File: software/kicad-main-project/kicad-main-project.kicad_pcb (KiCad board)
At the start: 2 copper layers, 1 part, among them U1 ESP32-DevKitC

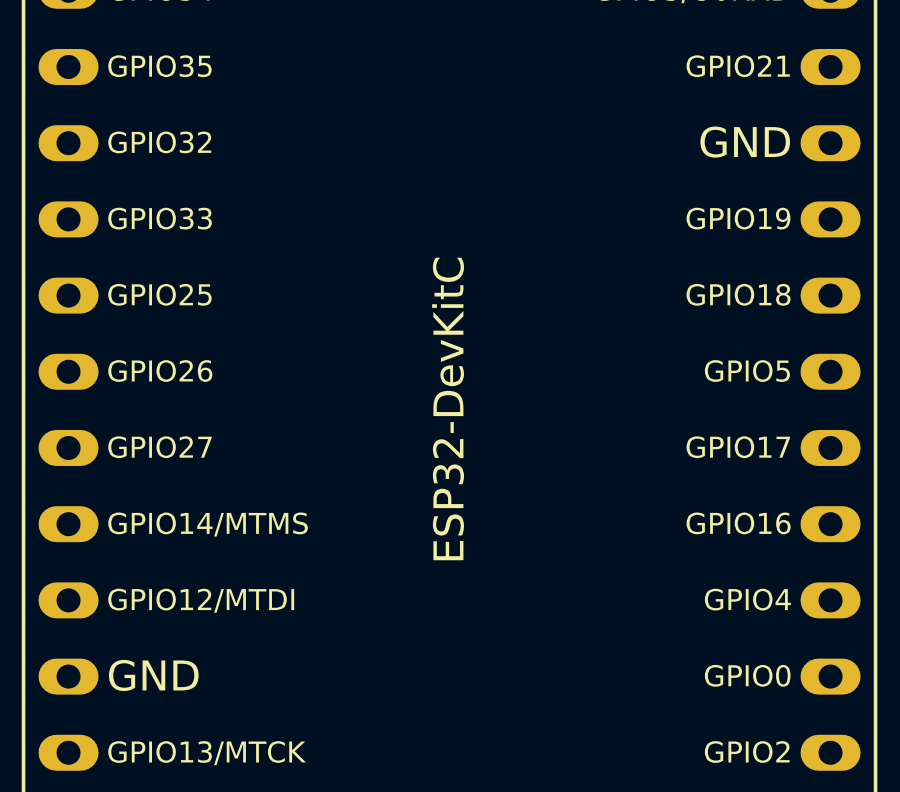
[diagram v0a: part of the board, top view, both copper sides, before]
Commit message: update schematic
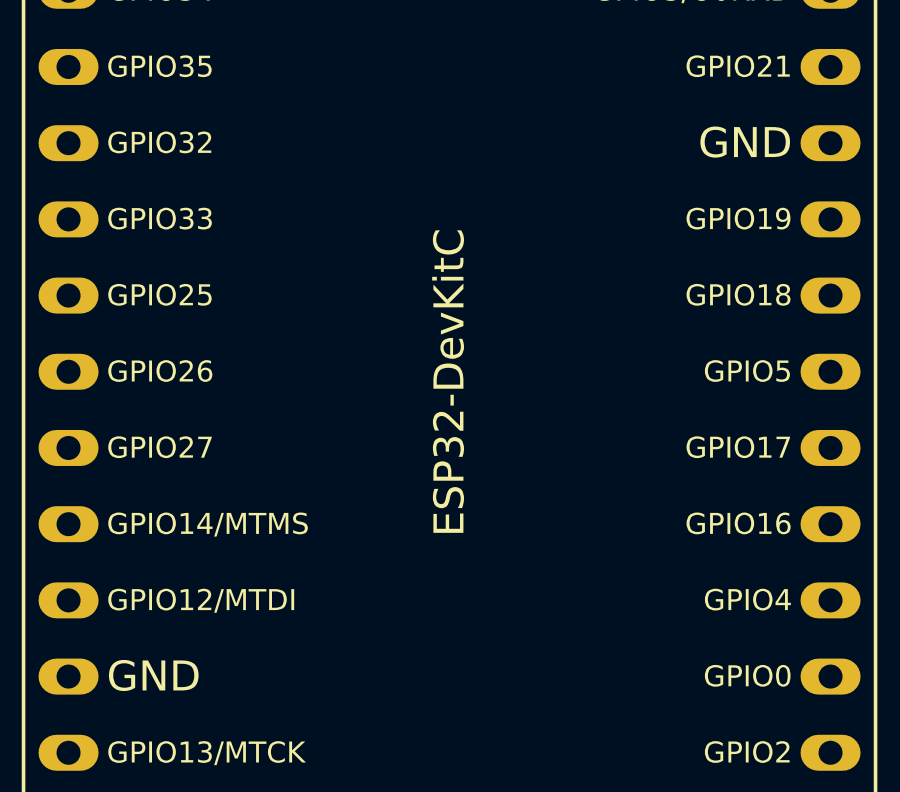
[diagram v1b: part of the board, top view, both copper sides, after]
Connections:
- net Net-(U1-GND-Pad14) renamed GND
- U1 pad 1: unconnected-(U1-3V3-Pad1) -> +3V3
- U1 pad 19: unconnected-(U1-5V-Pad19) -> +7.4V
- U1 pad 30: unconnected-(U1-GPIO18-Pad30) -> /AB
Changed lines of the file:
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@@
 	)
 	(net 0 "")
-	(net 1 "unconnected-(U1-5V-Pad19)")
-	(net 2 "Net-(U1-GND-Pad14)")
+	(net 1 "+7.4V")
+	(net 2 "GND")
 	(net 3 "unconnected-(U1-VDET_2{slash}GPIO35{slash}ADC1_CH7-Pad6)")
 	(net 4 "unconnected-(U1-GPIO19-Pad31)")
@@
 	(net 9 "unconnected-(U1-CMD-Pad18)")
 	(net 10 "unconnected-(U1-32K_XN{slash}GPIO33{slash}ADC1_CH5-Pad8)")
-	(net 11 "unconnected-(U1-3V3-Pad1)")
+	(net 11 "+3V3")
 	(net 12 "unconnected-(U1-SD_DATA0{slash}GPIO7-Pad21)")
 	(net 13 "unconnected-(U1-MTCK{slash}GPIO13{slash}ADC2_CH4-Pad15)")
@@
 	(net 34 "unconnected-(U1-VDET_1{slash}GPIO34{slash}ADC1_CH6-Pad5)")
 	(net 35 "unconnected-(U1-ADC2_CH7{slash}GPIO27-Pad11)")
-	(net 36 "unconnected-(U1-GPIO18-Pad30)")
+	(net 36 "/AB")
 	(footprint "Espressif:ESP32-DevKitC"
 		(layer "F.Cu")
@@
 		)
 		(property "Value" "ESP32-DevKitC"
-			(at 12.7 24.13 90)
+			(at 12.7 23.21728 90)
 			(layer "F.SilkS")
 			(effects
@@
 			(layers "*.Cu" "*.Mask")
 			(remove_unused_layers no)
-			(net 11 "unconnected-(U1-3V3-Pad1)")
+			(net 11 "+3V3")
 			(pinfunction "3V3")
 			(pintype "power_in")
@@
 			(layers "*.Cu" "*.Mask")
 			(remove_unused_layers no)
-			(net 2 "Net-(U1-GND-Pad14)")
+			(net 2 "GND")
 			(pinfunction "GND")
 			(pintype "power_in")
@@
 			(layers "*.Cu" "*.Mask")
 			(remove_unused_layers no)
-			(net 1 "unconnected-(U1-5V-Pad19)")
+			(net 1 "+7.4V")
 			(pinfunction "5V")
 			(pintype "power_in")
@@
 			(layers "*.Cu" "*.Mask")
 			(remove_unused_layers no)
-			(net 36 "unconnected-(U1-GPIO18-Pad30)")
+			(net 36 "/AB")
 			(pinfunction "GPIO18")
 			(pintype "bidirectional")
@@
 			(layers "*.Cu" "*.Mask")
 			(remove_unused_layers no)
-			(net 2 "Net-(U1-GND-Pad14)")
+			(net 2 "GND")
 			(pinfunction "GND")
 			(pintype "passive")
@@
 			(layers "*.Cu" "*.Mask")
 			(remove_unused_layers no)
-			(net 2 "Net-(U1-GND-Pad14)")
+			(net 2 "GND")
 			(pinfunction "GND")
 			(pintype "passive")

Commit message: update pcb
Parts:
- added BT1: Battery, Connector_JST:JST_XH_S2B-XH-A-1_1x02_P2.50mm_Horizontal, F.Cu at (90.8, 139.7)
- added C1: 100nF, Capacitor_THT:C_Disc_D3.0mm_W1.6mm_P2.50mm, F.Cu at (93.8, 101.0)
- added C2: 100nF, Capacitor_THT:C_Disc_D3.0mm_W1.6mm_P2.50mm, F.Cu at (93.5, 108.5)
- added C3: 100nF, Capacitor_THT:C_Disc_D3.0mm_W1.6mm_P2.50mm, F.Cu at (179.2, 100.0)
- added C4: 100nF, Capacitor_THT:C_Disc_D3.0mm_W1.6mm_P2.50mm, F.Cu at (179.2, 109.5)
- added C5: 10uF, Capacitor_THT:C_Disc_D3.0mm_W1.6mm_P2.50mm, F.Cu at (79.0, 77.0)
- added C6: 10uF, Capacitor_THT:C_Disc_D3.0mm_W1.6mm_P2.50mm, F.Cu at (188.8, 79.5)
- added J1: MOTOR_A, Connector_JST:JST_XH_S2B-XH-A-1_1x02_P2.50mm_Horizontal, F.Cu at (71.3, 142.2)
- added J2: MOTOR_B, Connector_JST:JST_XH_S2B-XH-A-1_1x02_P2.50mm_Horizontal, F.Cu at (208.7, 145.8)
- added R1: 10K, Resistor_THT:R_Axial_DIN0617_L17.0mm_D6.0mm_P25.40mm_Horizontal, F.Cu at (90.8, 92.5)
- added R2: 10K, Resistor_THT:R_Axial_DIN0617_L17.0mm_D6.0mm_P25.40mm_Horizontal, F.Cu at (90.8, 118.5)
- added R3: 10K, Resistor_THT:R_Axial_DIN0617_L17.0mm_D6.0mm_P25.40mm_Horizontal, F.Cu at (156.3, 92.0)
- added R4: 10K, Resistor_THT:R_Axial_DIN0617_L17.0mm_D6.0mm_P25.40mm_Horizontal, F.Cu at (157.6, 119.0)
- added SW1: SW_Push, Button_Switch_THT:SW_PUSH-12mm, F.Cu at (69.8, 94.0)
- added SW2: SW_Push, Button_Switch_THT:SW_PUSH-12mm, F.Cu at (70.0, 112.5)
- added SW3: SW_Push, Button_Switch_THT:SW_PUSH-12mm, F.Cu at (193.0, 92.0)
- added SW4: SW_Push, Button_Switch_THT:SW_PUSH-12mm, F.Cu at (194.0, 111.0)
- added U2: AMS117-5V, myAMS117-5V:Untitled, F.Cu at (119.0, 143.5)
- added U3: TB6612FNG, myTB6612FNG:Untitled, F.Cu at (154.0, 137.0)
- added U4: GP2Y0A02YK0F_1, Connector_JST:JST_XH_S3B-XH-A-1_1x03_P2.50mm_Horizontal, F.Cu at (97.5, 77.0)
- added U5: GP2Y0A02YK0F_2, Connector_JST:JST_XH_S3B-XH-A-1_1x03_P2.50mm_Horizontal, F.Cu at (174.5, 77.5)
- added U6: LCD-I2C, Connector_JST:JST_XH_S4B-XH-A_1x04_P2.50mm_Horizontal, F.Cu at (218.6, 117.8)
- added U7: CH340E, myCH340e:Untitled, F.Cu at (179.2, 135.7)
- moved U1 11.6 mm to (122.6, 76.9)
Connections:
- U1 pad 1: +3V3 -> unconnected-(U1-3V3-Pad1)
- U1 pad 23: unconnected-(U1-MTDO/GPIO15/ADC2_CH3-Pad23) -> AIN1
- U1 pad 24: unconnected-(U1-ADC2_CH2/GPIO2-Pad24) -> AIN2
- U1 pad 25: unconnected-(U1-GPIO0/BOOT/ADC2_CH1-Pad25) -> DTR
- U1 pad 27: unconnected-(U1-GPIO16-Pad27) -> BIN1
- U1 pad 28: unconnected-(U1-GPIO17-Pad28) -> BIN2
- U1 pad 3: unconnected-(U1-SENSOR_VP/GPIO36/ADC1_CH0-Pad3) -> Button_3
- U1 pad 30: /AB -> PWMA
- U1 pad 31: unconnected-(U1-GPIO19-Pad31) -> PWMB
- U1 pad 33: unconnected-(U1-GPIO21-Pad33) -> SDA
- U1 pad 34: unconnected-(U1-U0RXD/GPIO3-Pad34) -> TXD
- U1 pad 35: unconnected-(U1-U0TXD/GPIO1-Pad35) -> RXD
- U1 pad 36: unconnected-(U1-GPIO22-Pad36) -> SCL
- U1 pad 4: unconnected-(U1-SENSOR_VN/GPIO39/ADC1_CH3-Pad4) -> Button_4
- U1 pad 5: unconnected-(U1-VDET_1/GPIO34/ADC1_CH6-Pad5) -> Button_1
- U1 pad 6: unconnected-(U1-VDET_2/GPIO35/ADC1_CH7-Pad6) -> Button_2
- U1 pad 7: unconnected-(U1-32K_XP/GPIO32/ADC1_CH4-Pad7) -> GP2Y0A02YK0F_1
- U1 pad 8: unconnected-(U1-32K_XN/GPIO33/ADC1_CH5-Pad8) -> GP2Y0A02YK0F_2
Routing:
- net GND: track 0.00 -> 511.7 mm
- net +5v: track 0.00 -> 357.6 mm
- net Button_3: track 0.00 -> 130.1 mm
- net +7.4V: track 0.00 -> 121.7 mm
- net Button_4: track 0.00 -> 109.3 mm
- net GP2Y0A02YK0F_2: track 0.00 -> 92.5 mm
- net Net-(J1-Pin_2): track 0.00 -> 87.3 mm
- net TXD: track 0.00 -> 87.1 mm
- net Net-(J1-Pin_1): track 0.00 -> 83.9 mm
- net SCL: track 0.00 -> 83.8 mm
- net Button_2: track 0.00 -> 83.5 mm
- net SDA: track 0.00 -> 80.1 mm
- net GP2Y0A02YK0F_1: track 0.00 -> 66.8 mm
- net Button_1: track 0.00 -> 61.7 mm
- net Net-(J2-Pin_2): track 0.00 -> 59.4 mm
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
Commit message: update gerber + bom + image_
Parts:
- removed C5, C6: 10uF, Capacitor_THT:C_Disc_D3.0mm_W1.6mm_P2.50mm
- added REF**: MountingHole_3.7mm, MountingHole:MountingHole_3.7mm, F.Cu at (153.9, 50.7)
- added U10: K6-FALL-3, Connector_JST:JST_XH_S3B-XH-A-1_1x03_P2.50mm_Horizontal, F.Cu at (179.8, 63.5)
- added U8: AMS117-1.2V, myAMS117-5V:Untitled, F.Cu at (171.7, 74.7)
- added U9: K6-FALL-2, Connector_JST:JST_XH_S3B-XH-A-1_1x03_P2.50mm_Horizontal, F.Cu at (110.2, 57.0)
- R1, R2, R3, R4: footprint Resistor_THT:R_Axial_DIN0617_L17.0mm_D6.0mm_P25.40mm_Horizontal -> Resistor_THT:R_Axial_DIN0204_L3.6mm_D1.6mm_P2.54mm_Vertical
- U7: value CH340E -> K6-FALL-1; footprint myCH340e:Untitled -> Connector_JST:JST_XH_S3B-XH-A-1_1x03_P2.50mm_Horizontal
- moved BT1 121.3 mm to (198.8, 84.6), turned to 90 degrees
- moved U7 109.2 mm to (97.8, 63.0), turned to -155 degrees
- moved SW3 103.6 mm to (89.9, 81.8)
- moved C4 96.6 mm to (84.3, 91.7), turned to -90 degrees
- moved C3 89.9 mm to (93.0, 74.7), turned to 90 degrees
- moved SW4 86.3 mm to (108.7, 98.0)
- moved U2 84.1 mm to (186.9, 94.0), turned to 90 degrees
- moved R4 81.1 mm to (80.3, 94.5), turned to 90 degrees
- moved R3 75.3 mm to (82.3, 106.2)
- moved U3 48.2 mm to (171.2, 91.9)
- moved J1 43.9 mm to (107.2, 116.8), turned to 0 degrees
- moved U4 41.7 mm to (79.3, 114.5), turned to 0 degrees
- moved SW1 40.8 mm to (108.7, 81.8)
- moved U5 38.6 mm to (176.8, 116.0), turned to 0 degrees
- moved J2 37.1 mm to (198.8, 110.0)
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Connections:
- U1 pad 10: unconnected-(U1-DAC_2/ADC2_CH9/GPIO26-Pad10) -> K6-Fall-2
- U1 pad 11: unconnected-(U1-ADC2_CH7/GPIO27-Pad11) -> K6-Fall-3
- U1 pad 9: unconnected-(U1-DAC_1/ADC2_CH8/GPIO25-Pad9) -> K6-Fall-1
- U7 pad 1: GND -> +1.2v
- U7 pad 2: unconnected-(U7-+5V-Pad2) -> K6-Fall-1
- U7 pad 3: TXD -> GND
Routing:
- net +1.2v: track 0.00 -> 133.3 mm
- net +5v: track 357.6 -> 240.4 mm
- net TXD: track 87.1 -> 0.00 mm
- net K6-Fall-3: track 0.00 -> 75.0 mm
- net K6-Fall-1: track 0.00 -> 67.8 mm
- net K6-Fall-2: track 0.00 -> 61.0 mm
- net RXD: track 55.6 -> 0.00 mm
- net GP2Y0A02YK0F_2: track 92.5 -> 145.2 mm
- net DTR: track 40.1 -> 0.00 mm
- net PWMA: track 42.4 -> 12.3 mm
- net PWMB: track 51.3 -> 79.1 mm
- net Net-(J2-Pin_1): track 54.3 -> 26.8 mm
- net +7.4V: track 121.7 -> 146.3 mm
- net GP2Y0A02YK0F_1: track 66.8 -> 90.0 mm
- net SDA: track 80.1 -> 58.0 mm
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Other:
- board outline added: 135.1 x 80.9 mm
